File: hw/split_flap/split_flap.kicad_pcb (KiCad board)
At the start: 2 copper layers, 90 x 77.1 mm, 44 parts, among them J1 Conn_01x02, J10 Conn_01x05, J11 Conn_01x05, J12 Conn_01x05, J13 Conn_01x05, J14 Conn_01x05, J15 MOTOR_POWER, J16 JUMPER_MOTOR_5V, J17 EXPANDER_PORT, J19 POWER, J2 Conn_01x02, J21 Conn_01x05, J22 Conn_01x05, J3 Conn_01x02, J4 Conn_01x02, J5 Conn_01x02, J6 Conn_01x02, J7 Conn_01x02, J8 Conn_01x02, J9 Conn_01x05, U1 74HCT125, U10 ULN2803A, U14 ULN2803A, U2 NodeMCU_1.0_(ESP-12E), U3 74HC595, U4 PCF8574, U5 74HC595, U6 ULN2803A, U7 74HC595, U8 ULN2803A, U9 74HC595

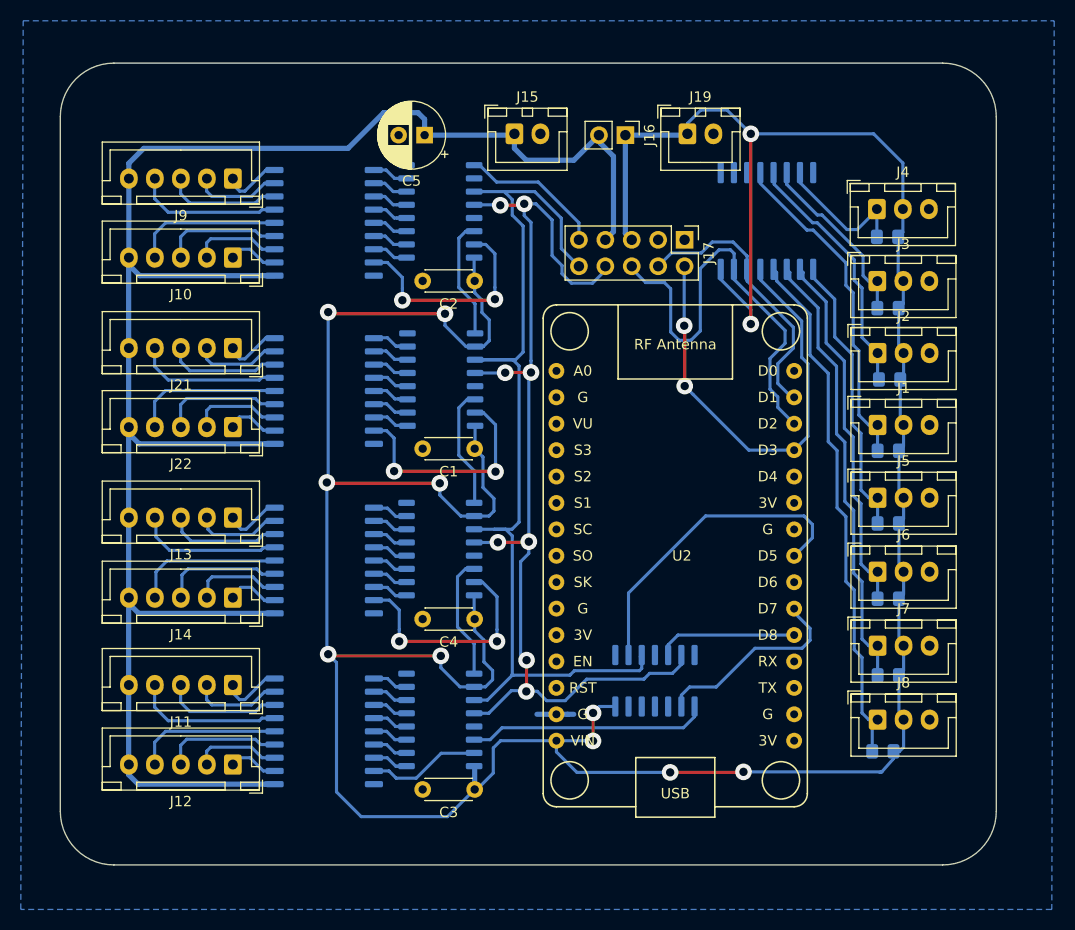
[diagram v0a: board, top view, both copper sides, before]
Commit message: Add mounting holes, logo and capacitor for +5V
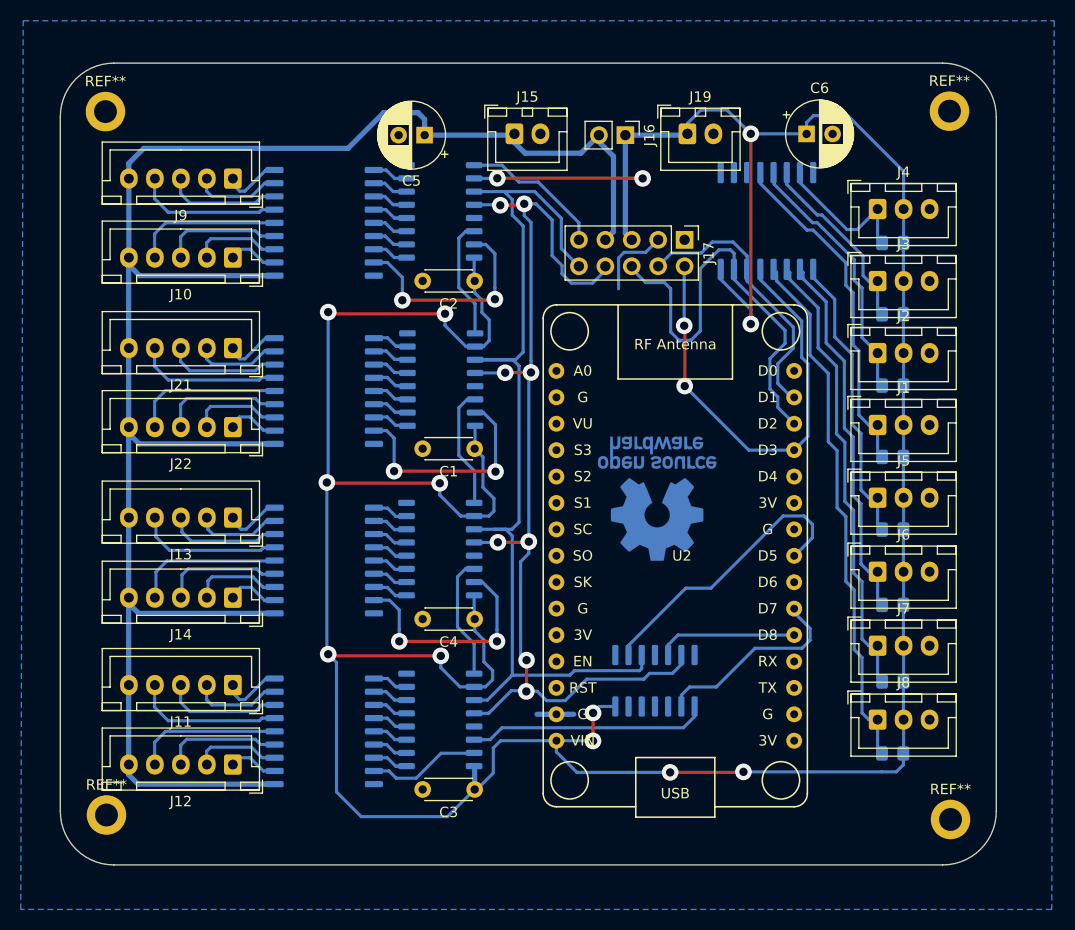
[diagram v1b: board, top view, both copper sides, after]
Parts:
- added C6: CP, Capacitor_THT:CP_Radial_D6.3mm_P2.50mm, F.Cu at (167.2, 61.9)
- added REF**: MountingHole_2.2mm_M2_DIN965_Pad, MountingHole:MountingHole_2.2mm_M2_DIN965_Pad, F.Cu at (99.7, 59.7)
- added REF**: MountingHole_2.2mm_M2_DIN965_Pad, MountingHole:MountingHole_2.2mm_M2_DIN965_Pad, F.Cu at (99.8, 127.3)
- added REF**: MountingHole_2.2mm_M2_DIN965_Pad, MountingHole:MountingHole_2.2mm_M2_DIN965_Pad, F.Cu at (181.0, 127.8)
- added REF**: MountingHole_2.2mm_M2_DIN965_Pad, MountingHole:MountingHole_2.2mm_M2_DIN965_Pad, F.Cu at (180.9, 59.7)
- added REF**: OSHW-Logo_11.4x12mm_Copper, Symbol:OSHW-Logo_11.4x12mm_Copper, B.Cu at (152.8, 96.9)
- moved R8 0.96 mm to (175.4, 121.4)
- moved R4 0.77 mm to (175.4, 72.3)
- moved R3 0.75 mm to (175.4, 79.2)
- moved R5 0.73 mm to (175.4, 99.9)
- moved R6 0.73 mm to (175.4, 107.1)
- moved R1 0.73 mm to (175.4, 92.9)
- moved R7 0.73 mm to (175.4, 114.5)
- moved R2 0.66 mm to (175.4, 86.1)
- moved J4 0.07 mm to (174.0, 69.1)
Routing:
- net +5V: track 325.6 -> 343.2 mm, vias 12 -> 14
- net GND: track 3.54 -> 11.0 mm
- net /SPI_3.3_CLK: track 30.8 -> 27.9 mm
- net Net-(J7-Pad1): track 42.8 -> 43.9 mm
- net Net-(J4-Pad1): track 13.6 -> 14.5 mm
- net VCC: track 182.7 -> 181.9 mm
- net Net-(J1-Pad1): track 31.2 -> 32.0 mm
- net Net-(J3-Pad1): track 17.3 -> 18.2 mm
- net Net-(J6-Pad1): track 35.2 -> 36.0 mm
- net Net-(J2-Pad1): track 24.3 -> 25.1 mm
- net Net-(J5-Pad1): track 26.7 -> 27.4 mm

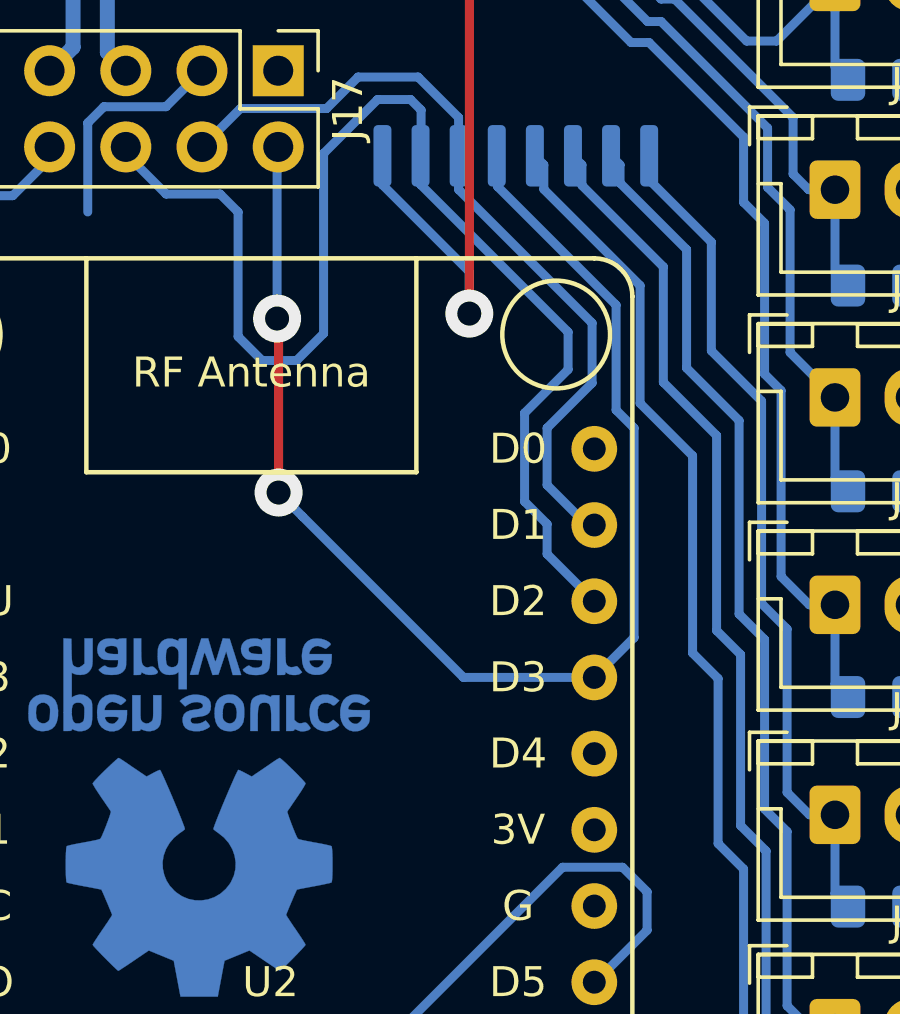
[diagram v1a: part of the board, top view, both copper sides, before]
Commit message: Add i2c pullup resistors on pcb...
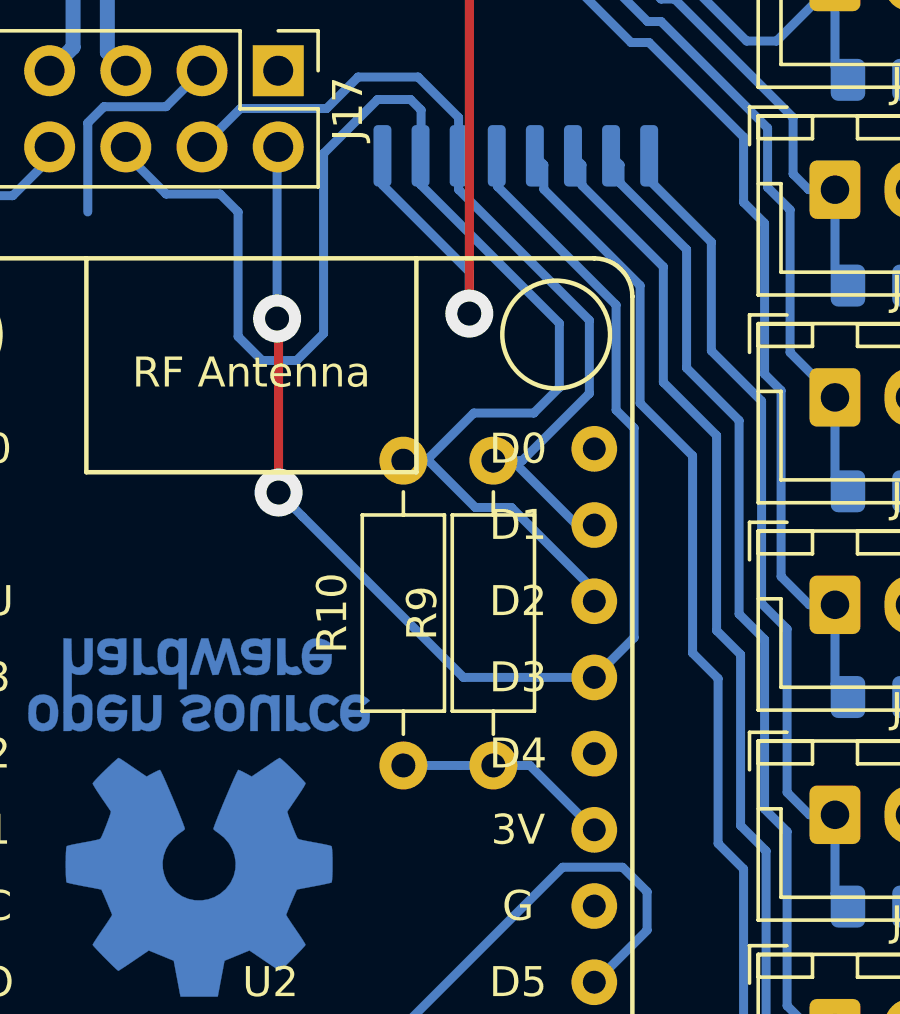
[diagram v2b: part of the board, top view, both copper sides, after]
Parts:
- added R10: R, Resistor_THT:R_Axial_DIN0207_L6.3mm_D2.5mm_P10.16mm_Horizontal, F.Cu at (159.6, 95.2)
- added R9: R, Resistor_THT:R_Axial_DIN0207_L6.3mm_D2.5mm_P10.16mm_Horizontal, F.Cu at (162.6, 95.2)
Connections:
- U1 pad 11: (no net) -> Net-(U1-Pad11)
- U2 pad 1: (no net) -> Net-(U2-Pad1)
- U2 pad 12: (no net) -> Net-(U2-Pad12)
- U2 pad 13: (no net) -> Net-(U2-Pad13)
- U2 pad 18: (no net) -> Net-(U2-Pad18)
- U2 pad 19: (no net) -> Net-(U2-Pad19)
- U2 pad 2: (no net) -> Net-(U2-Pad2)
- U2 pad 22: (no net) -> Net-(U2-Pad22)
- U2 pad 26: (no net) -> Net-(U2-Pad26)
- U2 pad 3: (no net) -> Net-(U2-Pad3)
- U2 pad 30: (no net) -> Net-(U2-Pad30)
- U2 pad 4: (no net) -> Net-(U2-Pad4)
- U2 pad 5: (no net) -> Net-(U2-Pad5)
- U2 pad 6: (no net) -> Net-(U2-Pad6)
- U2 pad 7: (no net) -> Net-(U2-Pad7)
- U2 pad 8: (no net) -> Net-(U2-Pad8)
- U2 pad 9: (no net) -> Net-(U2-Pad9)
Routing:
- net +3V3: track 0.00 -> 7.25 mm
- net /SDA: track 42.6 -> 48.5 mm
- net /SCL: track 26.9 -> 29.7 mm
